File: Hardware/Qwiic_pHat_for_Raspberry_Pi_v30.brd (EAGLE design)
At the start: 65 x 30.5 mm, 33 parts, among them J1 Qwiic Right Angle, J10 RASPBERRYPI-40-PIN-GPIO_PTH_N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, J7 Qwiic Right Angle, J8 Qwiic Right Angle

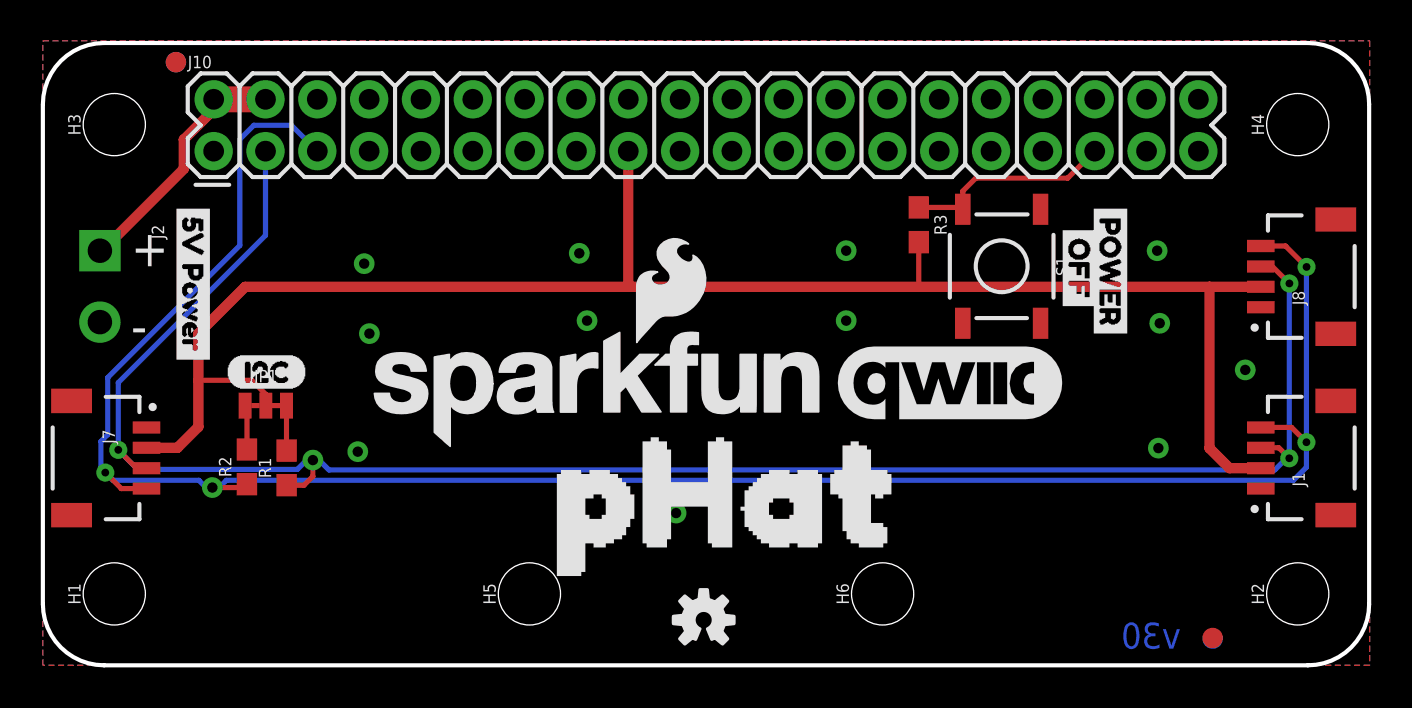
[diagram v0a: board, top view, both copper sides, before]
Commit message: Adds vertical Qwiic connectors to board
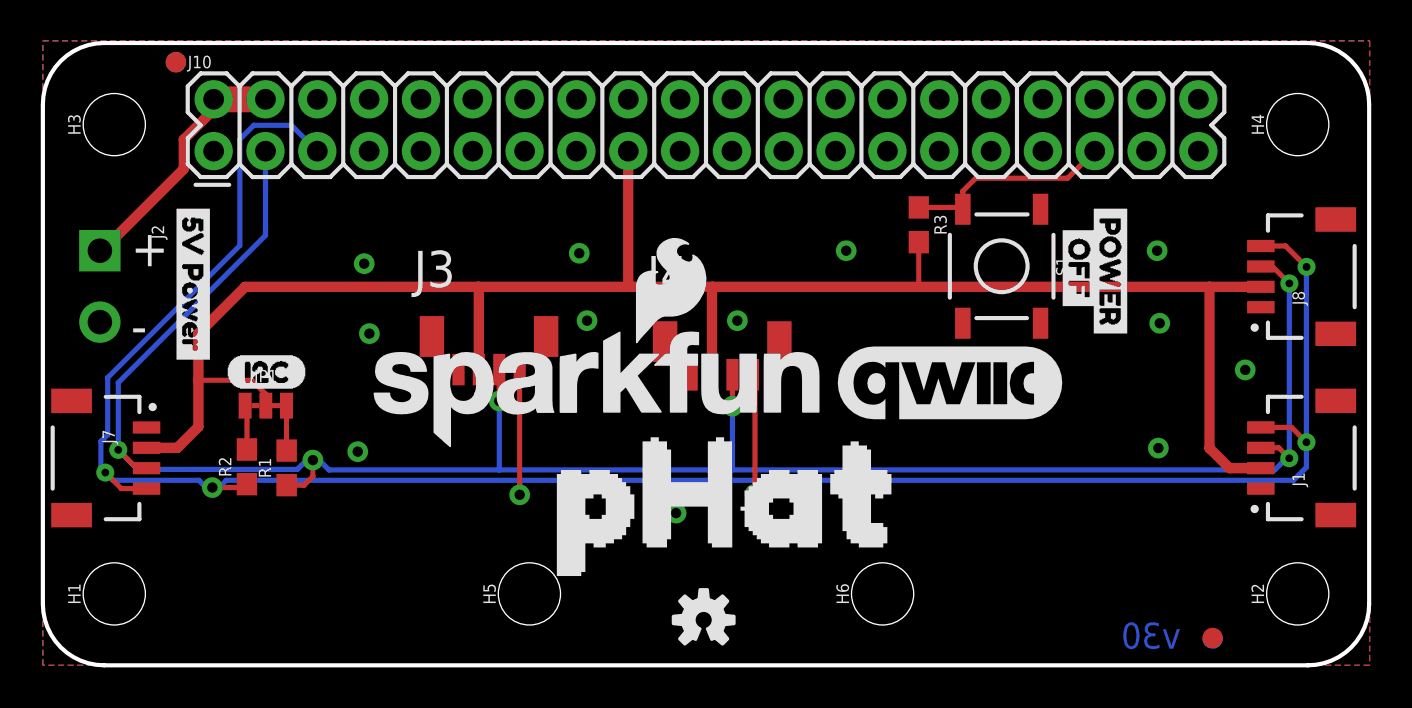
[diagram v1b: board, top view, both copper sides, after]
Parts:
- added J3, J4: (no value), SparkFun-Connectors:JST04_1MM_VERT
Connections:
- net 3.3V: now also J3.2, J4.2
- net GND: now also J3.1, J4.1
- net SCL: now also J3.4, J4.4
- net SDA: now also J3.3, J4.3
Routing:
- net SCL: track 102.6 -> 116.0 mm, vias 4 -> 6
- net SDA: track 92.0 -> 101.6 mm, vias 4 -> 6
- net 3.3V: track 84.4 -> 92.8 mm
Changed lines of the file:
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@@
 <drawing>
 <settings>
-<setting alwaysvectorfont="yes"/>
+<setting alwaysvectorfont="no"/>
 <setting keepoldvectorfont="yes"/>
 <setting verticaltext="up"/>
@@
 <layer number="19" name="Unrouted" color="6" fill="1" visible="yes" active="yes"/>
 <layer number="20" name="Dimension" color="15" fill="1" visible="yes" active="yes"/>
-<layer number="21" name="tPlace" color="16" fill="1" visible="yes" active="yes"/>
-<layer number="22" name="bPlace" color="14" fill="1" visible="yes" active="yes"/>
+<layer number="21" name="tPlace" color="16" fill="1" visible="no" active="yes"/>
+<layer number="22" name="bPlace" color="14" fill="1" visible="no" active="yes"/>
 <layer number="23" name="tOrigins" color="15" fill="1" visible="yes" active="yes"/>
 <layer number="24" name="bOrigins" color="15" fill="1" visible="yes" active="yes"/>
@@
 <element name="U$8" library="POWER" package="POWER2" value="" x="52.324" y="22.86" smashed="yes" rot="R270"/>
 <element name="U$9" library="POWER" package="OFF1" value="" x="50.8" y="21.844" smashed="yes" rot="R270"/>
+<element name="J3" library="SparkFun-Connectors" package="JST04_1MM_VERT" value="" x="20.066" y="13.716" smashed="yes">
+<attribute name="NAME" x="18.177" y="18.53633125" size="1.778" layer="25"/>
+<attribute name="PROD_ID" value="CONN-14483" x="20.066" y="13.716" size="1.778" layer="27" display="off"/>
+<attribute name="VALUE" x="18.177" y="10.89566875" size="1.778" layer="27"/>
+</element>
+<element name="J4" library="SparkFun-Connectors" package="JST04_1MM_VERT" value="" x="31.496" y="13.462" smashed="yes">
+<attribute name="NAME" x="29.607" y="18.28233125" size="1.778" layer="25"/>
+<attribute name="PROD_ID" value="CONN-14483" x="31.496" y="13.462" size="1.778" layer="27" display="off"/>
+<attribute name="VALUE" x="29.607" y="10.64166875" size="1.778" layer="27"/>
+</element>
 </elements>
 <signals>
@@
 <via x="26.289" y="20.193" extent="1-16" drill="0.508"/>
 <via x="26.67" y="16.891" extent="1-16" drill="0.508"/>
-<via x="39.37" y="16.891" extent="1-16" drill="0.508"/>
+<via x="34.036" y="16.891" extent="1-16" drill="0.508"/>
 <via x="39.37" y="20.32" extent="1-16" drill="0.508"/>
 <via x="15.432" y="10.471" extent="1-16" drill="0.508"/>
@@
 <contactref element="J2" pad="2"/>
 <contactref element="S1" pad="1"/>
+<contactref element="J4" pad="1"/>
+<contactref element="J3" pad="1"/>
 </signal>
 <signal name="3.3V">
@@
 <contactref element="R3" pad="2"/>
 <wire x1="57.1754" y1="18.55" x2="42.926" y2="18.55" width="0.508" layer="1"/>
-<wire x1="42.926" y1="18.55" x2="28.702" y2="18.55" width="0.508" layer="1"/>
-<wire x1="28.702" y1="18.55" x2="9.914" y2="18.55" width="0.508" layer="1"/>
+<wire x1="42.926" y1="18.55" x2="32.796" y2="18.55" width="0.508" layer="1"/>
+<wire x1="32.796" y1="18.55" x2="28.702" y2="18.55" width="0.508" layer="1"/>
+<wire x1="28.702" y1="18.55" x2="21.336" y2="18.55" width="0.508" layer="1"/>
+<wire x1="21.336" y1="18.55" x2="9.914" y2="18.55" width="0.508" layer="1"/>
 <wire x1="9.914" y1="18.55" x2="7.62" y2="16.256" width="0.508" layer="1"/>
 <wire x1="28.69" y1="18.562" x2="28.702" y2="18.55" width="0.508" layer="1"/>
 <wire x1="28.69" y1="25.2" x2="28.69" y2="18.562" width="0.508" layer="1"/>
 <wire x1="42.926" y1="20.74" x2="42.926" y2="18.55" width="0.254" layer="1"/>
+<contactref element="J3" pad="2"/>
+<contactref element="J4" pad="2"/>
+<wire x1="21.366" y1="14.491" x2="21.366" y2="18.52" width="0.508" layer="1"/>
+<wire x1="21.366" y1="18.52" x2="21.336" y2="18.55" width="0.508" layer="1"/>
+<wire x1="32.796" y1="14.237" x2="32.796" y2="18.55" width="0.508" layer="1"/>
 </signal>
 <signal name="SDA">
@@
 <contactref element="R1" pad="1"/>
 <wire x1="4.6536" y1="9.6012" x2="12.4714" y2="9.6012" width="0.254" layer="16"/>
-<wire x1="14.0208" y1="9.5758" x2="60.3758" y2="9.5758" width="0.254" layer="16"/>
+<wire x1="14.0208" y1="9.5758" x2="22.352" y2="9.5758" width="0.254" layer="16"/>
 <via x="13.2334" y="10.0584" extent="1-16" drill="0.508"/>
+<wire x1="22.352" y1="9.5758" x2="33.782" y2="9.5758" width="0.254" layer="16"/>
+<wire x1="33.782" y1="9.5758" x2="60.3758" y2="9.5758" width="0.254" layer="16"/>
 <wire x1="12.4714" y1="9.6012" x2="12.9286" y2="10.0584" width="0.254" layer="16"/>
 <wire x1="12.9286" y1="10.0584" x2="13.2334" y2="10.0584" width="0.254" layer="16"/>
@@
 <wire x1="3.6954" y1="13.8554" x2="3.6954" y2="10.5594" width="0.254" layer="16"/>
 <wire x1="10.91" y1="21.07" x2="3.6954" y2="13.8554" width="0.254" layer="16"/>
+<contactref element="J3" pad="3"/>
+<contactref element="J4" pad="3"/>
+<wire x1="22.366" y1="14.491" x2="22.366" y2="12.954" width="0.254" layer="1"/>
+<via x="22.366" y="12.954" extent="1-16" drill="0.508"/>
+<wire x1="22.366" y1="12.954" x2="22.366" y2="9.5898" width="0.254" layer="16"/>
+<wire x1="22.366" y1="9.5898" x2="22.352" y2="9.5758" width="0.254" layer="16"/>
+<wire x1="33.796" y1="14.236996875" x2="33.796" y2="12.700003125" width="0.254" layer="1"/>
+<via x="33.796" y="12.7" extent="1-16" drill="0.508"/>
+<wire x1="33.796" y1="12.7" x2="33.796" y2="9.5898" width="0.254" layer="16"/>
+<wire x1="33.796" y1="9.5898" x2="33.782" y2="9.5758" width="0.254" layer="16"/>
 </signal>
 <signal name="SCL">
@@
 <wire x1="8.9916" y1="9.0678" x2="8.636" y2="8.7122" width="0.254" layer="16"/>
 <wire x1="8.3058" y1="8.7122" x2="8.636" y2="8.7122" width="0.254" layer="16"/>
-<wire x1="8.9916" y1="9.0678" x2="61.2876" y2="9.0678" width="0.254" layer="16"/>
+<wire x1="8.9916" y1="9.0678" x2="23.368" y2="9.0678" width="0.254" layer="16"/>
 <via x="8.3058" y="8.7122" extent="1-16" drill="0.508"/>
+<wire x1="23.368" y1="9.0678" x2="34.8976" y2="9.0678" width="0.254" layer="16"/>
+<wire x1="34.897603125" y1="9.0678" x2="61.2876" y2="9.0678" width="0.254" layer="16"/>
 <wire x1="10" y1="8.8772" x2="9.835" y2="8.7122" width="0.254" layer="1"/>
 <wire x1="9.835" y1="8.7122" x2="8.3058" y2="8.7122" width="0.254" layer="1"/>
@@
 <wire x1="2.8448" y1="9.6592" x2="2.8448" y2="10.9728" width="0.254" layer="16"/>
 <wire x1="3.175" y1="14.097" x2="9.652" y2="20.574" width="0.254" layer="16"/>
+<contactref element="J3" pad="4"/>
+<contactref element="J4" pad="4"/>
+<wire x1="23.366" y1="14.491" x2="23.366" y2="8.3566" width="0.254" layer="1"/>
+<wire x1="23.366" y1="8.3566" x2="23.368" y2="8.3566" width="0.254" layer="1"/>
+<via x="23.368" y="8.3566" extent="1-16" drill="0.508"/>
+<wire x1="23.368" y1="8.3566" x2="23.368" y2="9.0678" width="0.254" layer="16"/>
+<via x="34.8976" y="8.382" extent="1-16" drill="0.508"/>
+<wire x1="34.8976" y1="8.382" x2="34.8976" y2="9.0678" width="0.254" layer="16"/>
+<wire x1="34.796" y1="14.237" x2="34.8976" y2="14.1354" width="0.254" layer="1"/>
+<wire x1="34.8976" y1="14.1354" x2="34.8976" y2="8.382" width="0.254" layer="1"/>
 </signal>
 <signal name="5V">

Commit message: Updates vertical qwiic connector footprint, recenters vertical qwiic connector.
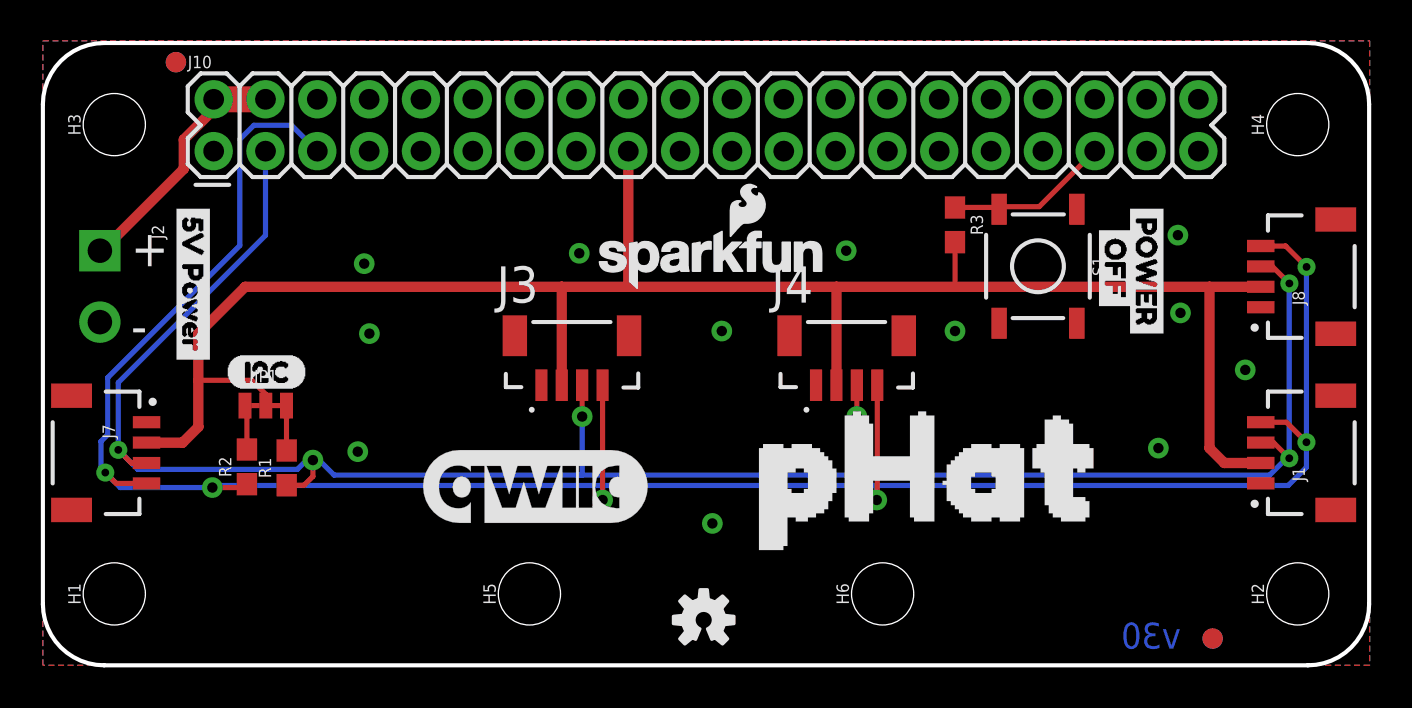
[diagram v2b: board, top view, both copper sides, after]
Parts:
- LOGO1: value SFE_LOGO_NAME_FLAME.2_INCH -> SFE_LOGO_NAME_FLAME.1_INCH; device SparkFun-Aesthetics:SFE_LOGO_NAME_FLAME_.2 -> SparkFun-Aesthetics:SFE_LOGO_NAME_FLAME_.1
- moved U$1 20.9 mm to (24.2, 8.72)
- moved U$3 9.99 mm to (30.3, 9.75)
- moved LOGO1 8.46 mm to (32.8, 19.9)
- moved J4 6.12 mm to (37.6, 13.0)
- moved J3 4.13 mm to (24.1, 13.0)
- moved U$9 1.78 mm to (52.6, 21.8)
- moved R3 1.78 mm to (44.7, 21.6)
- moved S1 1.78 mm to (48.8, 19.6)
- moved U$8 1.78 mm to (54.1, 22.9)
- moved J1 0.25 mm to (59.7, 10.4)
- moved J7 0.25 mm to (5.08, 10.4)
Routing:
- net D19: track 10.4 -> 8.06 mm
- net 3.3V: track 92.8 -> 93.8 mm
- net SCL: track 116.0 -> 115.3 mm
- net SDA: track 101.6 -> 101.0 mm

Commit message: Changes button and 5V power labels to text only, changes button text to "button" with gpio number
* Adds parallel 5V power through holes
* moves + and - silk
* moves button gpio pin to 17
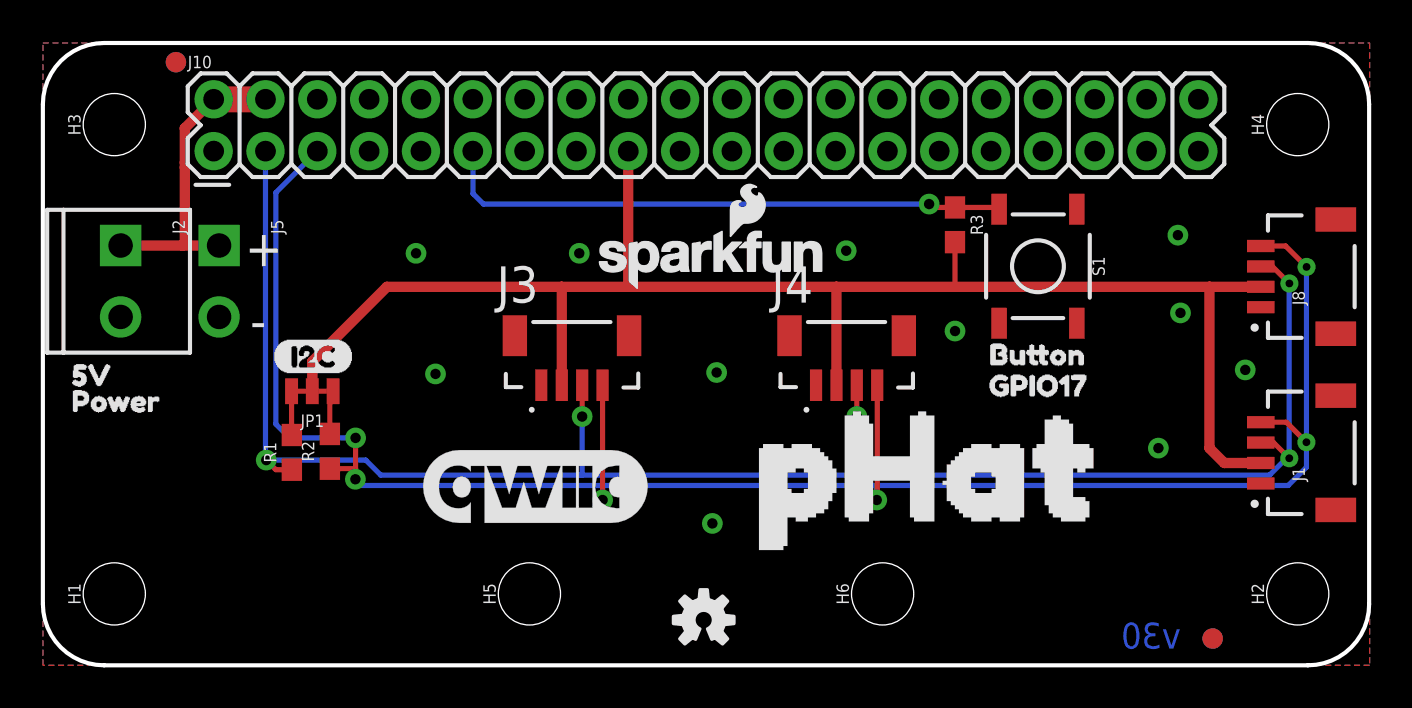
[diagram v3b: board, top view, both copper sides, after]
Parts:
- removed J7: Qwiic Right Angle, SparkFun-Connectors:JST04_1MM_RA
- added J5: (no value), SparkFun-Connectors:SCREWTERMINAL-3.5MM-2-NS
- added U$10: (no value), SparkFun-Aesthetics:SFE_LOGO_NAME_FLAME_.3
- J2: device SparkFun-Connectors:SCREWTERMINAL-3.5MM-2-NS -> SparkFun-Connectors:SCREWTERMINAL-3.5MM-2
- U$6: device buzzard_labels:5V_POWER0 -> All labels:5V0
- U$7: device buzzard_labels:5V_POWER0 -> All labels:POWER1
- U$8: device POWER:POWER2 -> All labels:BUTTON2
- U$9: device POWER:OFF1 -> All labels:GPIO173
- moved U$8 11.5 mm to (45.5, 15.2), turned to 0 degrees
- moved U$6 11.0 mm to (0.51, 14.2), turned to 0 degrees
- moved U$9 10.8 mm to (45.5, 13.7), turned to 0 degrees
- moved U$7 7.03 mm to (0.51, 13.0), flipped to the top, turned to 0 degrees
- moved R2 4.13 mm to (14.1, 10.5)
- moved U$2 2.41 mm to (11.2, 15.1)
- moved JP1 2.39 mm to (13.2, 13.4), turned to 180 degrees
- moved J2 1.05 mm to (3.81, 20.6)
- moved R1 0.80 mm to (12.2, 10.4)
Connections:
- net 3.3V: no longer J7.2
- net 5V: now also J5.1
- net D17: now also R3.1, S1.3
- net D19: no longer R3.1, S1.3
- net GND: now also J5.2; no longer J7.1
- net SCL: no longer J7.4
- net SDA: no longer J7.3
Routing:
- net D17: track 0.00 -> 28.2 mm, vias 0 -> 1
- net SCL: track 115.3 -> 96.6 mm
- net 3.3V: track 93.8 -> 78.7 mm
- net SDA: track 101.0 -> 88.3 mm, vias 6 -> 5
- net D19: track 8.06 -> 0.00 mm
- net 5V: track 12.3 -> 15.2 mm

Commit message: Adjusts 5V Power silk, changes button name in schematic
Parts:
- added U$11: (no value), All labels:5V0
- added U$12: (no value), All labels:POWER1
- S1: value POWER_OFF -> BUTTON GPI017
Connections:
- net D17 renamed BUTTON/D17
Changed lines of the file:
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@@
 <layer number="115" name="ReferenceISLANDS" color="7" fill="1" visible="no" active="yes"/>
 <layer number="116" name="Patch_BOT" color="9" fill="4" visible="no" active="yes"/>
-<layer number="117" name="PM_Ref" color="26" fill="1" visible="no" active="yes"/>
+<layer number="117" name="PM_Ref" color="26" fill="1" visible="yes" active="yes"/>
 <layer number="118" name="Rect_Pads" color="7" fill="1" visible="no" active="yes"/>
-<layer number="119" name="PF_Ref" color="31" fill="1" visible="no" active="yes"/>
-<layer number="120" name="WFL_Ref" color="25" fill="1" visible="no" active="yes"/>
+<layer number="119" name="PF_Ref" color="31" fill="1" visible="yes" active="yes"/>
+<layer number="120" name="WFL_Ref" color="25" fill="1" visible="yes" active="yes"/>
 <layer number="121" name="_tsilk" color="7" fill="1" visible="no" active="yes"/>
 <layer number="122" name="_bsilk" color="7" fill="1" visible="no" active="yes"/>
@@
 <text x="9.906" y="19.558" size="1.778" layer="21" font="vector" ratio="15">+</text>
 <text x="10.16" y="16.002" size="1.778" layer="21" font="vector" ratio="15">-</text>
-<text x="11.176" y="19.558" size="1.778" layer="22" font="vector" ratio="15" rot="MR0">+</text>
-<text x="11.43" y="16.002" size="1.778" layer="22" font="vector" ratio="15" rot="MR0">-</text>
+<text x="7.112" y="19.558" size="1.778" layer="22" font="vector" ratio="15" rot="MR0">+</text>
+<text x="7.112" y="16.002" size="1.778" layer="22" font="vector" ratio="15" rot="MR0">-</text>
 </plain>
 <attributes>
@@
 <attribute name="VALUE" x="5.08" y="21.844" size="0.6096" layer="27" font="vector" ratio="20" rot="R270"/>
 </element>
-<element name="S1" library="SparkFun-Switches" package="TACTILE_SWITCH_SMD_5.2MM" value="POWER_OFF" x="48.768" y="19.558" smashed="yes" rot="R270">
+<element name="S1" library="SparkFun-Switches" package="TACTILE_SWITCH_SMD_5.2MM" value="BUTTON GPI017" x="48.768" y="19.558" smashed="yes" rot="R270">
 <attribute name="NAME" x="51.435" y="19.558" size="0.6096" layer="25" font="vector" ratio="20" rot="R270" align="bottom-center"/>
 <attribute name="PROD_ID" value="SWCH-14139" x="48.768" y="19.558" size="1.778" layer="27" font="vector" ratio="15" rot="R270" display="off"/>
@@
 <element name="U$9" library="All labels" package="GPIO173" value="" x="45.466" y="13.716" smashed="yes"/>
 <element name="U$10" library="SparkFun-Aesthetics" package="SFE_LOGO_NAME_FLAME_.3" value="" x="32.258" y="11.684" smashed="yes" rot="MR0"/>
+<element name="U$11" library="All labels" package="5V0" value="" x="6.604" y="14.224" smashed="yes" rot="MR0"/>
+<element name="U$12" library="All labels" package="POWER1" value="" x="6.604" y="12.954" smashed="yes" rot="MR0"/>
 </elements>
 <signals>
@@
 <contactref element="J10" pad="36"/>
 </signal>
-<signal name="D17">
+<signal name="BUTTON/D17">
 <contactref element="J10" pad="11"/>
 <contactref element="S1" pad="3"/>
